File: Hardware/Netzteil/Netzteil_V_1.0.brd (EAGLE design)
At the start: 110.2 x 102.9 mm, 29 parts, among them IC1 7812L, IC3 LM2574HVN-5.0, IC4 LM2574HVN-3.3, X1 87758-1016

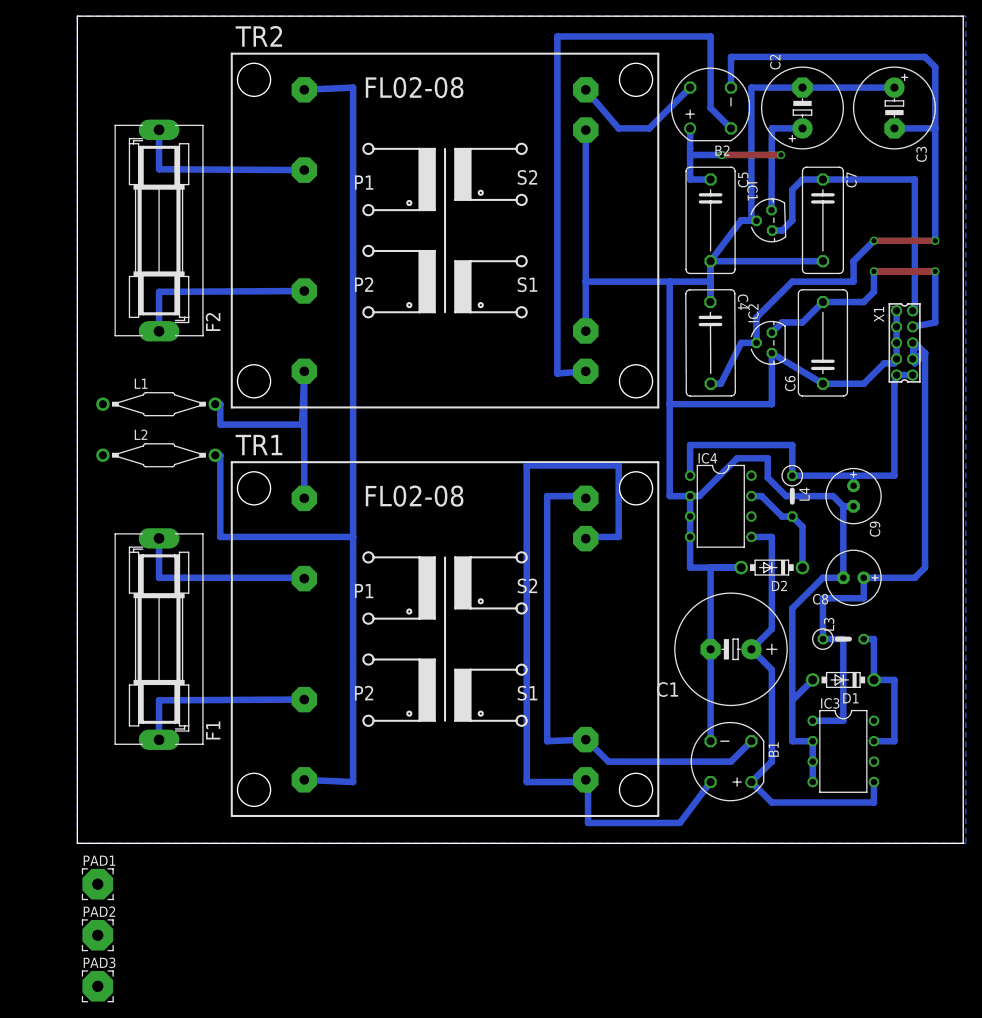
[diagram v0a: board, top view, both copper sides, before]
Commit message: Letzte Änderungen an Netzteil, OP und IP Board
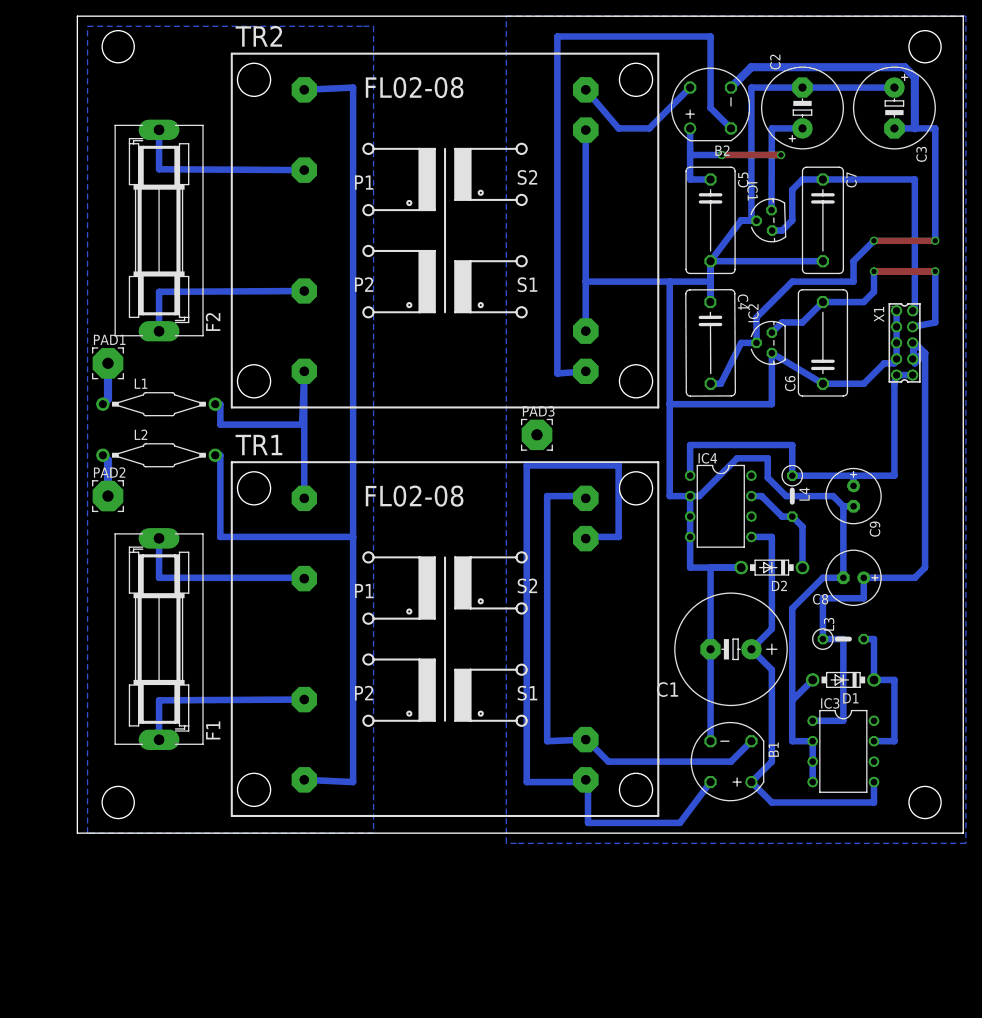
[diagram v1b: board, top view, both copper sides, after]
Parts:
- moved PAD3 87.7 mm to (64.8, 55.9)
- moved PAD1 64.8 mm to (11.4, 64.8)
- moved PAD2 54.6 mm to (11.4, 48.3)
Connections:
- net N$15 renamed -12V
- net N$17 renamed +12V
- net N$19 renamed 3V3
- net N$22 renamed 5V
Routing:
- net N$6: track 96.1 -> 89.5 mm
- net N$20: track 0.00 -> 5.34 mm
- net N$18: track 0.00 -> 5.34 mm
- added copper zone on layer 16, net EA
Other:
- board size 110.2 x 102.9 mm -> 110.2 x 101.6 mm

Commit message: Minor Board Fixes
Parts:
- moved C1 9.92 mm to (81.3, 22.9)
- moved C4 9.92 mm to (78.7, 61.0)
- moved C6 9.92 mm to (92.7, 61.0)
- moved C8 9.92 mm to (96.5, 31.8)
- moved C9 9.92 mm to (96.5, 41.9)
- moved IC2 9.92 mm to (86.4, 61.0)
- moved IC3 9.92 mm to (95.2, 10.2)
- moved L3 9.92 mm to (95.2, 24.1)
- moved TR1 9.92 mm to (45.7, 24.1)
- moved B1 9.92 mm to (81.3, 8.89)
- moved D1 9.92 mm to (95.2, 19.1)
- moved F1 9.92 mm to (10.2, 24.1)
- moved L2 9.92 mm to (10.2, 47.0)
- moved B2 9.92 mm to (78.7, 90.2)
- moved C2 9.92 mm to (90.2, 90.2)
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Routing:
- net N$3: track 94.7 -> 47.1 mm
- net 5V: track 73.9 -> 68.3 mm
- net GND: track 292.7 -> 291.2 mm
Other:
- board text added: "Teslacontroller Netzteil Rev 1.0 05/19"
